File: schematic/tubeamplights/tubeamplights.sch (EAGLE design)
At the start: 5 parts

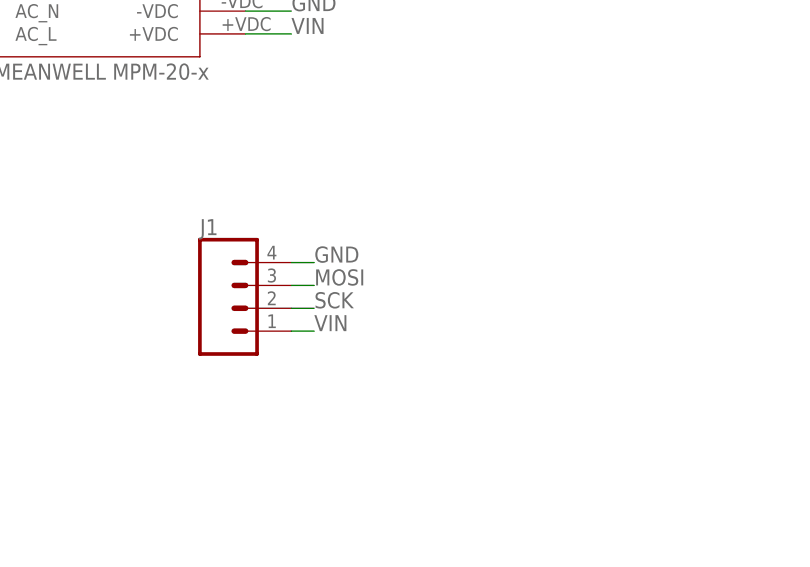
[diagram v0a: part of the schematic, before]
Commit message: Fix the reg footprint
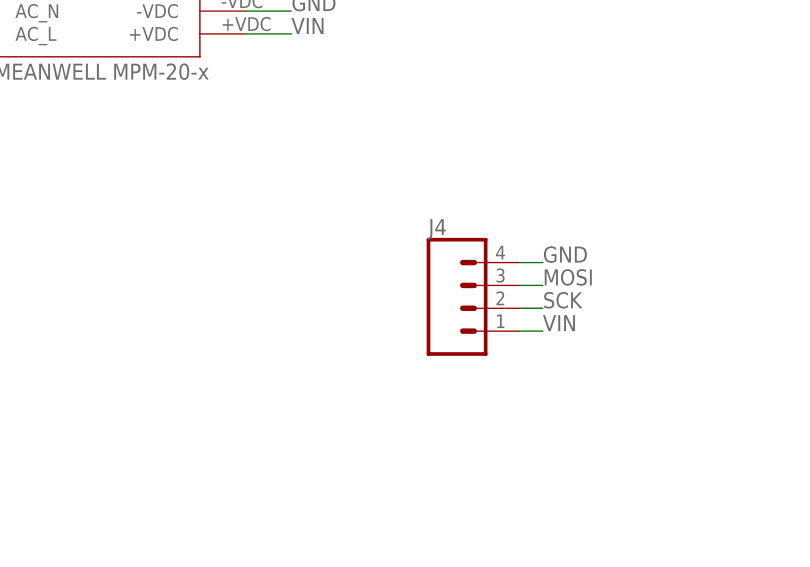
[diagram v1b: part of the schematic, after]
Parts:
- removed J1: (no value), SparkFun-Connectors:CONN_04JST-PTH-VERT
- added J4: (no value), SparkFun-Connectors:CONN_04
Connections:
- net GND: now also J4.4; no longer J1.4
- net MOSI: now also J4.3; no longer J1.3
- net SCK: now also J4.2; no longer J1.2
- net VIN: now also J4.1; no longer J1.1
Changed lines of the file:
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@@
 <part name="FRAME1" library="ChrisD" deviceset="FRAME-LETTER" device=""/>
 <part name="U$2" library="meanwell-mpm-20-x" deviceset="MPM-20-X" device=""/>
-<part name="J1" library="SparkFun-Connectors" library_urn="urn:adsk.eagle:library:513" deviceset="CONN_04" device="JST-PTH-VERT" package3d_urn="urn:adsk.eagle:package:38102/1"/>
 <part name="J2" library="SparkFun-Connectors" library_urn="urn:adsk.eagle:library:513" deviceset="CONN_01" device="PTH_2MM" package3d_urn="urn:adsk.eagle:package:38029/1"/>
 <part name="J3" library="SparkFun-Connectors" library_urn="urn:adsk.eagle:library:513" deviceset="CONN_01" device="PTH_2MM" package3d_urn="urn:adsk.eagle:package:38029/1"/>
+<part name="J4" library="SparkFun-Connectors" library_urn="urn:adsk.eagle:library:513" deviceset="CONN_04" device="" package3d_urn="urn:adsk.eagle:package:38085/1"/>
 </parts>
 <sheets>
@@
 </instance>
 <instance part="U$2" gate="G$1" x="60.96" y="86.36" smashed="yes"/>
-<instance part="J1" gate="G$1" x="88.9" y="58.42" smashed="yes">
-<attribute name="VALUE" x="83.82" y="51.054" size="1.778" layer="96" font="vector"/>
-<attribute name="NAME" x="83.82" y="66.548" size="1.778" layer="95" font="vector"/>
-</instance>
 <instance part="J2" gate="G$1" x="20.32" y="116.84" smashed="yes">
 <attribute name="VALUE" x="17.78" y="112.014" size="1.778" layer="96" font="vector"/>
@@
 <attribute name="VALUE" x="17.78" y="101.854" size="1.778" layer="96" font="vector"/>
 <attribute name="NAME" x="17.78" y="109.728" size="1.778" layer="95" font="vector"/>
+</instance>
+<instance part="J4" gate="G$1" x="114.3" y="58.42" smashed="yes">
+<attribute name="VALUE" x="109.22" y="51.054" size="1.778" layer="96" font="vector"/>
+<attribute name="NAME" x="109.22" y="66.548" size="1.778" layer="95" font="vector"/>
 </instance>
 </instances>
@@
 </segment>
 <segment>
-<pinref part="J1" gate="G$1" pin="1"/>
-<wire x1="93.98" y1="55.88" x2="96.52" y2="55.88" width="0.1524" layer="91"/>
-<label x="96.52" y="55.88" size="1.778" layer="95"/>
+<pinref part="J4" gate="G$1" pin="1"/>
+<wire x1="119.38" y1="55.88" x2="121.92" y2="55.88" width="0.1524" layer="91"/>
+<label x="121.92" y="55.88" size="1.778" layer="95"/>
 </segment>
 </net>
@@
 </segment>
 <segment>
-<pinref part="J1" gate="G$1" pin="4"/>
-<wire x1="93.98" y1="63.5" x2="96.52" y2="63.5" width="0.1524" layer="91"/>
-<label x="96.52" y="63.5" size="1.778" layer="95"/>
+<pinref part="J4" gate="G$1" pin="4"/>
+<wire x1="119.38" y1="63.5" x2="121.92" y2="63.5" width="0.1524" layer="91"/>
+<label x="121.92" y="63.5" size="1.778" layer="95"/>
 </segment>
 </net>
@@
 </segment>
 <segment>
-<pinref part="J1" gate="G$1" pin="2"/>
-<wire x1="93.98" y1="58.42" x2="96.52" y2="58.42" width="0.1524" layer="91"/>
-<label x="96.52" y="58.42" size="1.778" layer="95"/>
+<pinref part="J4" gate="G$1" pin="2"/>
+<wire x1="119.38" y1="58.42" x2="121.92" y2="58.42" width="0.1524" layer="91"/>
+<label x="121.92" y="58.42" size="1.778" layer="95"/>
 </segment>
 </net>
@@
 </segment>
 <segment>
-<pinref part="J1" gate="G$1" pin="3"/>
-<wire x1="93.98" y1="60.96" x2="96.52" y2="60.96" width="0.1524" layer="91"/>
-<label x="96.52" y="60.96" size="1.778" layer="95"/>
+<pinref part="J4" gate="G$1" pin="3"/>
+<wire x1="119.38" y1="60.96" x2="121.92" y2="60.96" width="0.1524" layer="91"/>
+<label x="121.92" y="60.96" size="1.778" layer="95"/>
 </segment>
 </net>
